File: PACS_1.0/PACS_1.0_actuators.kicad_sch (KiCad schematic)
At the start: 5 parts, among them J2 Conn_01x02_Pin

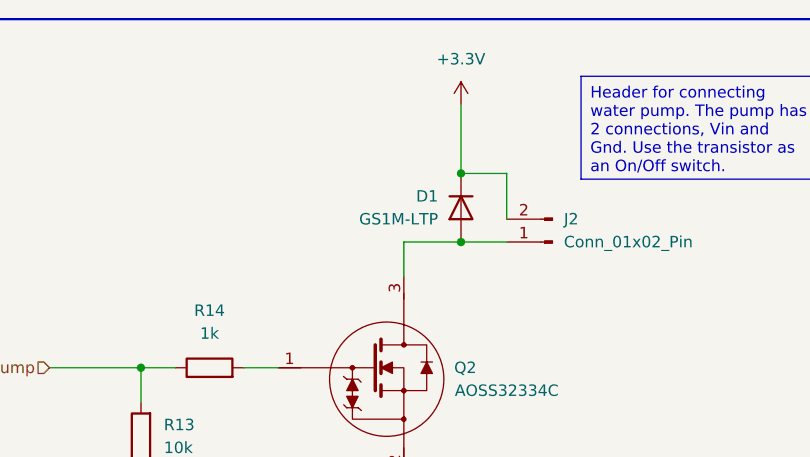
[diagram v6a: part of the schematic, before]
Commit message: added more footprints
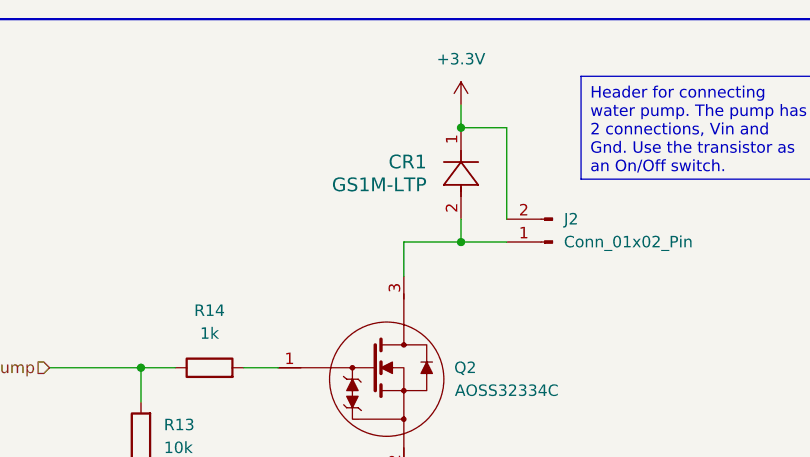
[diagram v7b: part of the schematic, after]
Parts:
- removed D1: GS1M-LTP, symbol Device:D
- added CR1: GS1M-LTP, Diode_SMD:D_SMA, symbol GS1M-LTP:GS1M-LTP
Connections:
- net +3.3V: now also CR1.1
- net at J2.1 (Pin_1), Q2.3: now also CR1.2
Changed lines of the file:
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@@
+	)
+	(junction
+		(at 147.32 86.36)
+		(diameter 0)
+		(color 0 0 0 0)
 	)
 	(junction
@@
 	)
 	(junction
-		(at 147.32 86.36)
-		(diameter 0)
-		(color 0 0 0 0)
-	)
-	(junction
-		(at 147.32 78.74)
+		(at 147.32 73.66)
 		(diameter 0)
 		(color 0 0 0 0)
@@
 	(wire
 		(pts
-			(xy 152.4 83.82) (xy 152.4 78.74)
+			(xy 152.4 73.66) (xy 147.32 73.66)
+		)
+		(stroke
+			(width 0)
+			(type default)
+		)
+	)
+	(wire
+		(pts
+			(xy 152.4 73.66) (xy 152.4 83.82)
 		)
 		(stroke
@@
 	(wire
 		(pts
-			(xy 152.4 78.74) (xy 147.32 78.74)
-		)
-		(stroke
-			(width 0)
-			(type default)
-		)
-	)
-	(wire
-		(pts
 			(xy 111.76 115.57) (xy 140.97 115.57)
 		)
@@
 	(wire
 		(pts
-			(xy 152.4 86.36) (xy 147.32 86.36)
-		)
-		(stroke
-			(width 0)
-			(type default)
-		)
-	)
-	(wire
-		(pts
 			(xy 101.6 100.33) (xy 111.76 100.33)
 		)
@@
 	(wire
 		(pts
-			(xy 147.32 86.36) (xy 140.97 86.36)
-		)
-		(stroke
-			(width 0)
-			(type default)
-		)
-	)
-	(wire
-		(pts
-			(xy 147.32 71.12) (xy 147.32 78.74)
+			(xy 140.97 86.36) (xy 147.32 86.36)
 		)
 		(stroke
@@
 		(pts
 			(xy 111.76 100.33) (xy 111.76 104.14)
+		)
+		(stroke
+			(width 0)
+			(type default)
+		)
+	)
+	(wire
+		(pts
+			(xy 147.32 71.12) (xy 147.32 73.66)
+		)
+		(stroke
+			(width 0)
+			(type default)
+		)
+	)
+	(wire
+		(pts
+			(xy 147.32 86.36) (xy 152.4 86.36)
+		)
+		(stroke
+			(width 0)
+			(type default)
+		)
+	)
+	(wire
+		(pts
+			(xy 147.32 83.82) (xy 147.32 86.36)
 		)
 		(stroke
@@
 	)
 	(symbol
+		(lib_id "GS1M-LTP:GS1M-LTP")
+		(at 147.32 83.82 90)
+		(unit 1)
+		(exclude_from_sim no)
+		(in_bom yes)
+		(on_board yes)
+		(dnp no)
+		(property "Reference" "CR1"
+			(at 143.51 77.4699 90)
+			(effects
+				(font
+					(size 1.524 1.524)
+				)
+				(justify left)
+			)
+		)
+		(property "Value" "GS1M-LTP"
+			(at 143.51 80.0099 90)
+			(effects
+				(font
+					(size 1.524 1.524)
+				)
+				(justify left)
+			)
+		)
+		(property "Footprint" "Diode_SMD:D_SMA"
+			(at 147.32 83.82 0)
+			(effects
+				(font
+					(size 1.27 1.27)
+					(italic yes)
+				)
+				(hide yes)
+			)
+		)
+		(property "Datasheet" "GS1M-LTP"
+			(at 147.32 83.82 0)
+			(effects
+				(font
+					(size 1.27 1.27)
+					(italic yes)
+				)
+				(hide yes)
+			)
+		)
+		(property "Description" ""
+			(at 147.32 83.82 0)
+			(effects
+				(font
+					(size 1.27 1.27)
+				)
+				(hide yes)
+			)
+		)
+		(pin "2"
+		)
+		(pin "1"
+		)
+		(instances
+			(project ""
+				(path "/6996cbc8-fffb-40fd-8350-2bb7d19e6e7a/2328e835-669b-4c27-8f58-8619ea15ff21"
+					(reference "CR1")
+					(unit 1)
+				)
+			)
+		)
+	)
+	(symbol
 		(lib_id "Connector:Conn_01x02_Pin")
 		(at 157.48 86.36 180)
@@
 					(unit 1)
 				)
-			)
-		)
-	)
-	(symbol
-		(lib_id "Device:D")
-		(at 147.32 82.55 90)
-		(mirror x)
-		(unit 1)
-		(exclude_from_sim no)
-		(in_bom yes)
-		(on_board yes)
-		(dnp no)
-		(property "Reference" "D1"
-			(at 144.78 81.2799 90)
-			(effects
-				(font
-					(size 1.27 1.27)
-				)
-				(justify left)
-			)
-		)
-		(property "Value" "GS1M-LTP"
-			(at 144.78 83.8199 90)
-			(effects
-				(font
-					(size 1.27 1.27)
-				)
-				(justify left)
-			)
-		)
-		(property "Footprint" ""
-			(at 147.32 82.55 0)
-			(effects
-				(font
-					(size 1.27 1.27)
-				)
-				(hide yes)
-			)
-		)
-		(property "Datasheet" "~"
-			(at 147.32 82.55 0)
-			(effects
-				(font
-					(size 1.27 1.27)
-				)
-				(hide yes)
-			)
-		)
-		(property "Description" "Diode"
-			(at 147.32 82.55 0)
-			(effects
-				(font
-					(size 1.27 1.27)
-				)
-				(hide yes)
-			)
-		)
-		(property "Sim.Device" "D"
-			(at 147.32 82.55 0)
-			(effects
-				(font
-					(size 1.27 1.27)
-				)
-				(hide yes)
-			)
-		)
-		(property "Sim.Pins" "1=K 2=A"
-			(at 147.32 82.55 0)
-			(effects
-				(font
-					(size 1.27 1.27)
-				)
-				(hide yes)
-			)
-		)
-		(pin "1"
-		)
-		(pin "2"
-		)
-		(instances
-			(project "PACS_1.0"
-				(path "/6996cbc8-fffb-40fd-8350-2bb7d19e6e7a/2328e835-669b-4c27-8f58-8619ea15ff21"
-					(reference "D1")
-					(unit 1)
-				)

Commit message: Started the PCB design
added several footprints, need to find footprint for Xbee, need to add traces for GND and power
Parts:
- J2: footprint (none) -> Connector_JST:JST_EH_B2B-EH-A_1x02_P2.50mm_Vertical
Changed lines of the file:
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@@
 			)
 		)
-		(property "Footprint" ""
+		(property "Footprint" "Connector_JST:JST_EH_B2B-EH-A_1x02_P2.50mm_Vertical"
 			(at 157.48 86.36 0)
 			(effects
